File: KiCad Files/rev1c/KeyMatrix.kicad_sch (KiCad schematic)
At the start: 97 parts, among them SW1 SW_Push, SW10 SW_Push, SW11 SW_Push, SW12 SW_Push, SW13 SW_Push, SW14 SW_Push, SW15 SW_Push, SW16 SW_Push, SW17 SW_Push, SW18 SW_Push, SW19 SW_Push, SW2 SW_Push, SW20 SW_Push, SW21 SW_Push, SW22 SW_Push, SW23 SW_Push, SW24 SW_Push, SW25 SW_Push, SW26 SW_Push, SW27 SW_Push, SW28 SW_Push, SW29 SW_Push, SW3 SW_Push, SW30 SW_Push, SW31 SW_Push, SW32 SW_Push, SW33 SW_Push, SW34 SW_Push, SW35 SW_Push, SW36 SW_Push, SW37 SW_Push, SW38 SW_Push, SW39 SW_Push, SW4 SW_Push, SW40 SW_Push, SW41 SW_Push, SW42 SW_Push, SW43 SW_Push, SW44 SW_Push, SW45 SW_Push, SW46 SW_Push, SW47 SW_Push, SW48 SW_Push, SW49 SW_Push, SW5 SW_Push, SW50 SW_Push, SW51 SW_Push, SW52 SW_Push, SW53 SW_Push, SW54 SW_Push, SW55 SW_Push, SW56 SW_Push, SW57 SW_Push, SW58 SW_Push, SW59 SW_Push, SW6 SW_Push, SW60 SW_Push, SW63 SW_Push, SW65 SW_Push, SW66 SW_Push, SW67 SW_Push, SW68 SW_Push, SW7 SW_Push, SW8 SW_Push, SW9 SW_Push

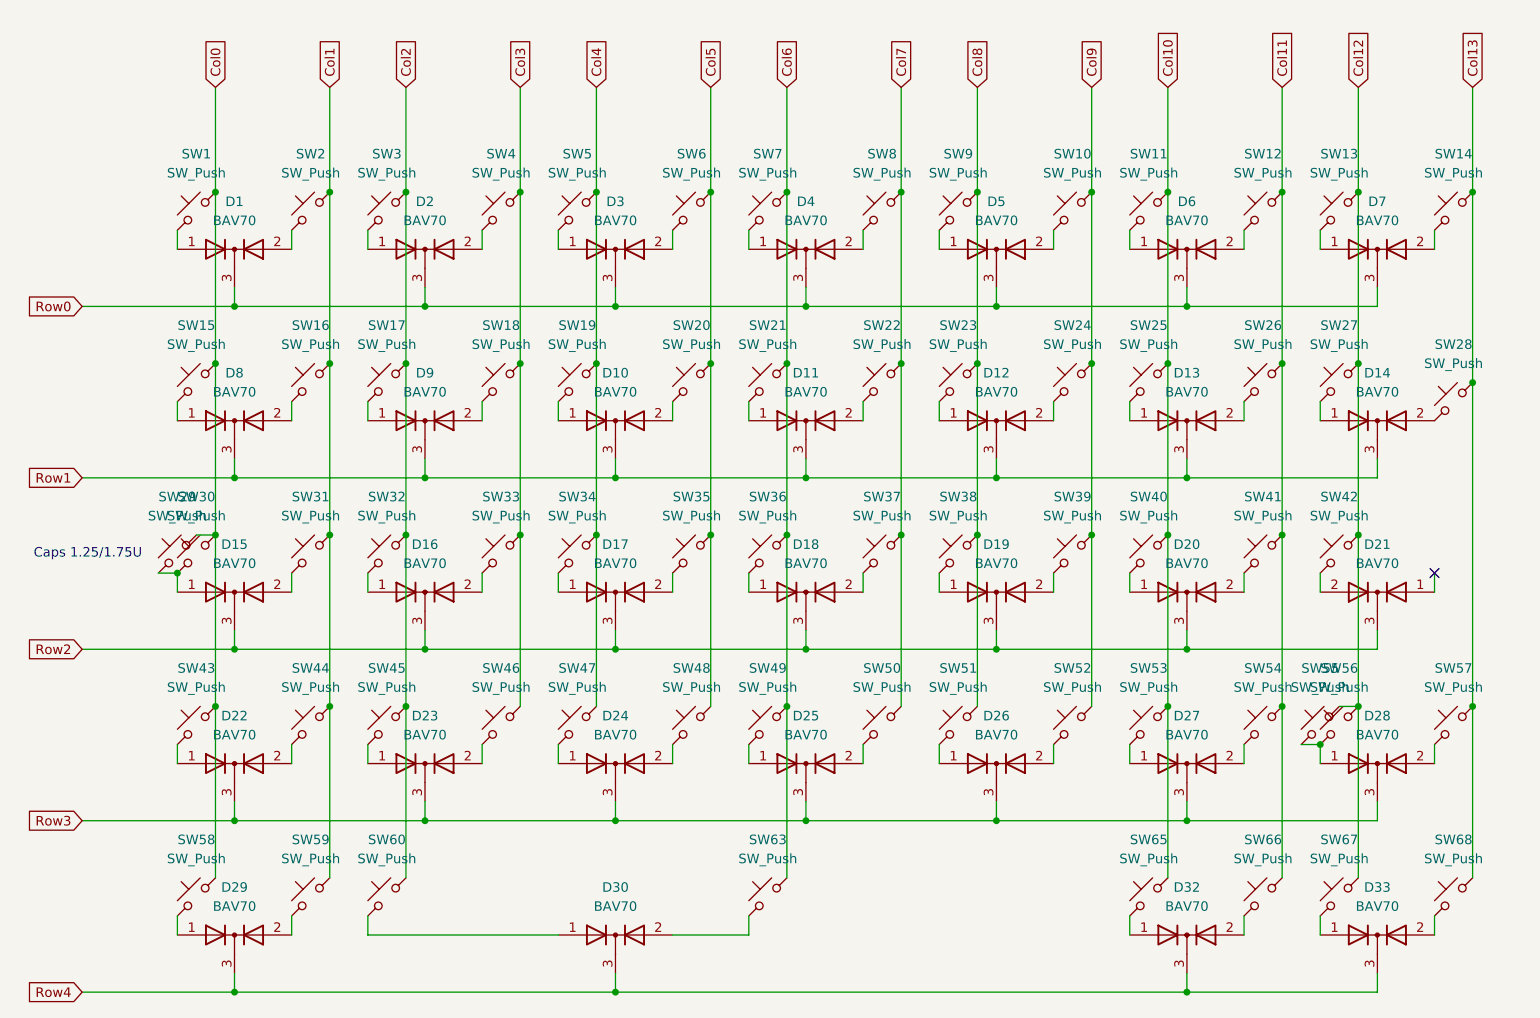
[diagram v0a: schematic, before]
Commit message: Rev1c preliminarty update
Changes to Schematic:
- Added switches to support different layouts
- Added One BAV70 to support said switches

Changes to PCB:
- Imported changes from schematic, placed some of the switches but needs more work
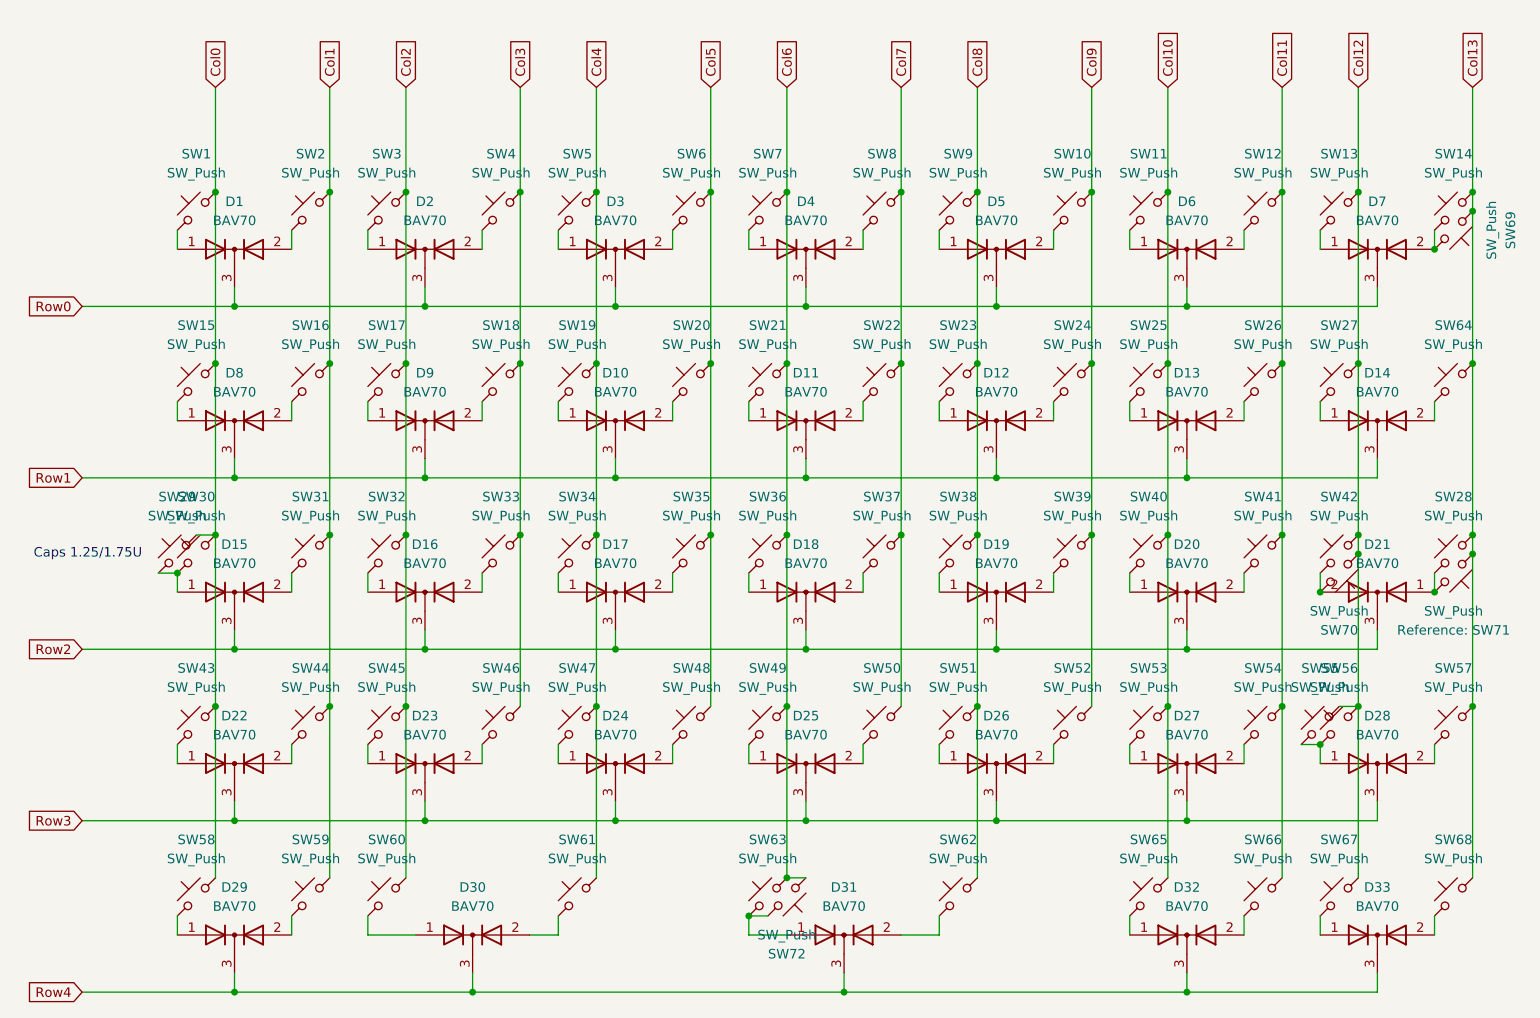
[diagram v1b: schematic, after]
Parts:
- added D31: BAV70, PCM_Package_TO_SOT_SMD_AKL:SOT-23, symbol Diode:BAV70
- added SW61: SW_Push, PCM_Switch_Keyboard_Hotswap_Kailh:SW_Hotswap_Kailh_MX_Plated_2.75u, symbol Switch:SW_Push_45deg
- added SW62, SW71: SW_Push, PCM_Switch_Keyboard_Hotswap_Kailh:SW_Hotswap_Kailh_MX_Plated_2.25u, symbol Switch:SW_Push_45deg
- added SW64, SW69: SW_Push, PCM_Switch_Keyboard_Hotswap_Kailh:SW_Hotswap_Kailh_MX_Plated_1.00u, symbol Switch:SW_Push_45deg
- added SW70: SW_Push, PCM_Switch_Keyboard_Hotswap_Kailh:SW_Hotswap_Kailh_MX_Plated_1.50u, symbol Switch:SW_Push_45deg
- added SW72: SW_Push, PCM_Switch_Keyboard_Hotswap_Kailh:SW_Hotswap_Kailh_MX_Plated_1.25u, symbol Switch:SW_Push_45deg
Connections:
- net Col12: now also SW70.2
- net Col13: now also SW64.1, SW69.1, SW71.2
- net Col4: now also SW61.1
- net Col6: now also SW72.2
- net Col8: now also SW62.1
- net Row4: now also D31.3 (K)
- net at D7.2 (A), SW14.2: now also SW69.2
- net at D30.2 (A): now also SW61.2; no longer SW63.2
- net at SW28.2: now also D21.1 (A), SW71.1; no longer D14.2 (A)
- net at D21.2 (A), SW42.2: now also SW70.1
- new net: D31.2 (A), SW62.2
- new net: D14.2 (A), SW64.2
- new net: D31.1 (A), SW63.2, SW72.1
- no-connect marks 1 -> 0
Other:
- moved on the sheet: D30, SW28

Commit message: update on pcb
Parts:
- removed SW70: SW_Push, PCM_Switch_Keyboard_Hotswap_Kailh:SW_Hotswap_Kailh_MX_Plated_1.50u, symbol Switch:SW_Push_45deg
- removed SW71: SW_Push, PCM_Switch_Keyboard_Hotswap_Kailh:SW_Hotswap_Kailh_MX_Plated_2.25u, symbol Switch:SW_Push_45deg

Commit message: Updates
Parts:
- SW61: footprint PCM_Switch_Keyboard_Hotswap_Kailh:SW_Hotswap_Kailh_MX_Plated_2.75u -> PCM_Switch_Keyboard_Hotswap_Kailh:SW_Hotswap_Kailh_MX_Plated_1.25u
- SW72: footprint PCM_Switch_Keyboard_Hotswap_Kailh:SW_Hotswap_Kailh_MX_Plated_1.25u -> PCM_Switch_Keyboard_Hotswap_Kailh:SW_Hotswap_Kailh_MX_Plated_2.75u
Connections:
- net Col6: now also SW72.1; no longer SW72.2
- net at D31.1 (A), SW63.2: now also SW72.2; no longer SW72.1
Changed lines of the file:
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@@
 	)
 	(junction
-		(at 144.78 137.16)
-		(diameter 0)
-		(color 0 0 0 0)
-	)
-	(junction
 		(at 220.98 91.44)
 		(diameter 0)
@@
 	)
 	(junction
+		(at 144.78 137.16)
+		(diameter 0)
+		(color 0 0 0 0)
+	)
+	(junction
 		(at 170.18 68.58)
 		(diameter 0)
@@
 	)
 	(junction
+		(at 139.7 142.24)
+		(diameter 0)
+		(color 0 0 0 0)
+	)
+	(junction
 		(at 134.62 68.58)
 		(diameter 0)
@@
 	)
 	(junction
-		(at 139.7 142.24)
-		(diameter 0)
-		(color 0 0 0 0)
-	)
-	(junction
 		(at 220.98 114.3)
 		(diameter 0)
@@
 	(wire
 		(pts
+			(xy 144.78 137.16) (xy 147.32 137.16)
+		)
+		(stroke
+			(width 0)
+			(type default)
+		)
+	)
+	(wire
+		(pts
 			(xy 83.82 114.3) (xy 83.82 137.16)
 		)
@@
 	(wire
 		(pts
-			(xy 139.7 142.24) (xy 142.24 142.24)
-		)
-		(stroke
-			(width 0)
-			(type default)
-		)
-	)
-	(wire
-		(pts
 			(xy 114.3 50.8) (xy 114.3 53.34)
 		)
@@
 	(wire
 		(pts
+			(xy 139.7 142.24) (xy 142.24 142.24)
+		)
+		(stroke
+			(width 0)
+			(type default)
+		)
+	)
+	(wire
+		(pts
 			(xy 50.8 152.4) (xy 71.12 152.4)
 		)
@@
 	(wire
 		(pts
-			(xy 144.78 137.16) (xy 147.32 137.16)
-		)
-		(stroke
-			(width 0)
-			(type default)
-		)
-	)
-	(wire
-		(pts
 			(xy 205.74 73.66) (xy 205.74 76.2)
 		)
@@
 			)
 		)
-		(property "Footprint" "PCM_Switch_Keyboard_Hotswap_Kailh:SW_Hotswap_Kailh_MX_Plated_2.75u"
+		(property "Footprint" "PCM_Switch_Keyboard_Hotswap_Kailh:SW_Hotswap_Kailh_MX_Plated_1.25u"
 			(at 116.84 139.7 0)
 			(effects
@@
 		(lib_id "Switch:SW_Push_45deg")
 		(at 144.78 139.7 0)
-		(mirror x)
+		(mirror y)
 		(unit 1)
 		(exclude_from_sim no)
@@
 		(dnp no)
 		(property "Reference" "SW72"
-			(at 144.78 147.32 0)
+			(at 144.78 132.08 0)
 			(effects
 				(font
@@
 		)
 		(property "Value" "SW_Push"
-			(at 144.78 144.78 0)
+			(at 144.78 134.62 0)
 			(effects
 				(font
@@
 			)
 		)
-		(property "Footprint" "PCM_Switch_Keyboard_Hotswap_Kailh:SW_Hotswap_Kailh_MX_Plated_1.25u"
+		(property "Footprint" "PCM_Switch_Keyboard_Hotswap_Kailh:SW_Hotswap_Kailh_MX_Plated_2.75u"
 			(at 144.78 139.7 0)
 			(effects
